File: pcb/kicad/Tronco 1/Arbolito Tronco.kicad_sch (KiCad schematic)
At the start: 18 parts, among them U1 WS2812B, U10 WS2812B, U11 WS2812B, U12 WS2812B, U2 WS2812B, U3 WS2812B, U4 WS2812B, U5 WS2812B, U6 WS2812B, U7 WS2812B, U8 WS2812B, U9 WS2812B

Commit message: Do some cleaning and add .gitignore
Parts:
- removed U10, U3, U4, U9: WS2812B, LED_SMD:LED_WS2812B_PLCC4_5.0x5.0mm_P3.2mm, symbol WB2182:WS2812B
- added J1, J2, J3, J4, J5, J6: Conn_01x01, Library:Input, symbol Connector_Generic:Conn_01x01
- added J10, J11, J12, J7, J8, J9: Conn_01x01, Library:Output, symbol Connector_Generic:Conn_01x01
- U1, U2: footprint LED_SMD:LED_WS2812B_PLCC4_5.0x5.0mm_P3.2mm -> Library:LED_WS2812B_PLCC4_5.0x5.0mm_P3.2mm
- U3: renamed from U5; footprint LED_SMD:LED_WS2812B_PLCC4_5.0x5.0mm_P3.2mm -> Library:LED_WS2812B_PLCC4_5.0x5.0mm_P3.2mm
- U4: renamed from U6; footprint LED_SMD:LED_WS2812B_PLCC4_5.0x5.0mm_P3.2mm -> Library:LED_WS2812B_PLCC4_5.0x5.0mm_P3.2mm
- U5: renamed from U7; footprint LED_SMD:LED_WS2812B_PLCC4_5.0x5.0mm_P3.2mm -> Library:LED_WS2812B_PLCC4_5.0x5.0mm_P3.2mm
- U6: renamed from U8; footprint LED_SMD:LED_WS2812B_PLCC4_5.0x5.0mm_P3.2mm -> Library:LED_WS2812B_PLCC4_5.0x5.0mm_P3.2mm
- U7: renamed from U11; footprint LED_SMD:LED_WS2812B_PLCC4_5.0x5.0mm_P3.2mm -> Library:LED_WS2812B_PLCC4_5.0x5.0mm_P3.2mm
- U8: renamed from U12; footprint LED_SMD:LED_WS2812B_PLCC4_5.0x5.0mm_P3.2mm -> Library:LED_WS2812B_PLCC4_5.0x5.0mm_P3.2mm
- renumbered C11 to C1, C12 to C2, C13 to C3, C14 to C4, C15 to C5, C16 to C6
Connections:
- net +5V: now also J10.1 (Pin_1), J3.1 (Pin_1), J4.1 (Pin_1), J9.1 (Pin_1)
- net DIN: now also J1.1 (Pin_1), J2.1 (Pin_1)
- net Dout: now also J7.1 (Pin_1), J8.1 (Pin_1)
- net GND: now also J11.1 (Pin_1), J12.1 (Pin_1), J5.1 (Pin_1), J6.1 (Pin_1)
- net at U2.2 (DOUT): now also U3.4 (DIN)
- net at U6.2 (DOUT): now also U7.4 (DIN)

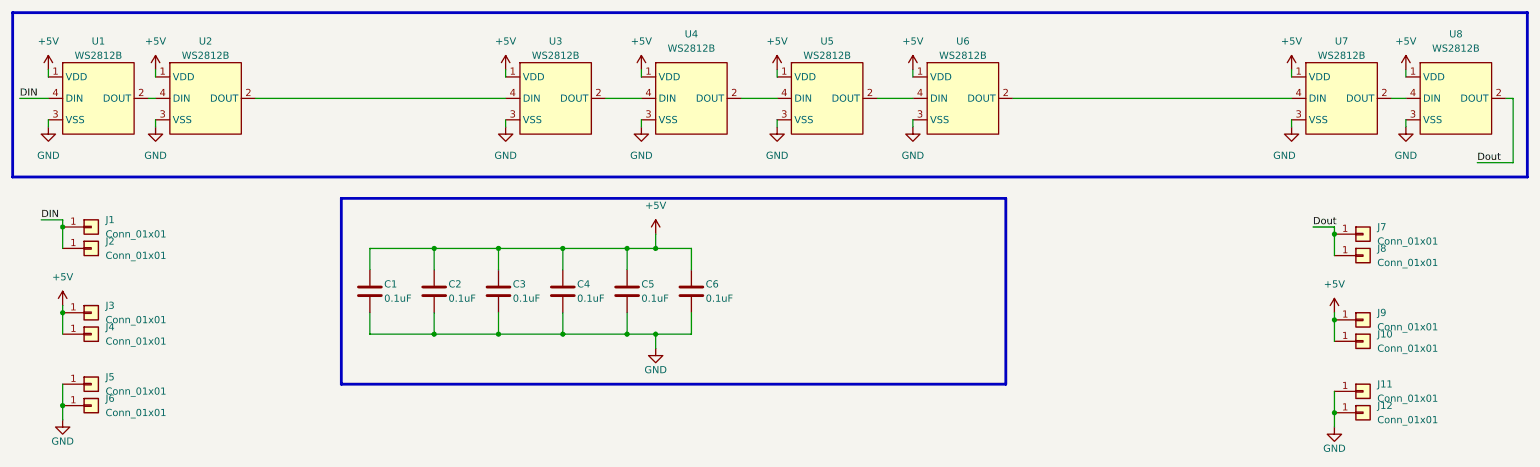
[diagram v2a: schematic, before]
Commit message: DRC Errors fixeds
The WS218B double footprint was remade in order to avoid DRC errors :3
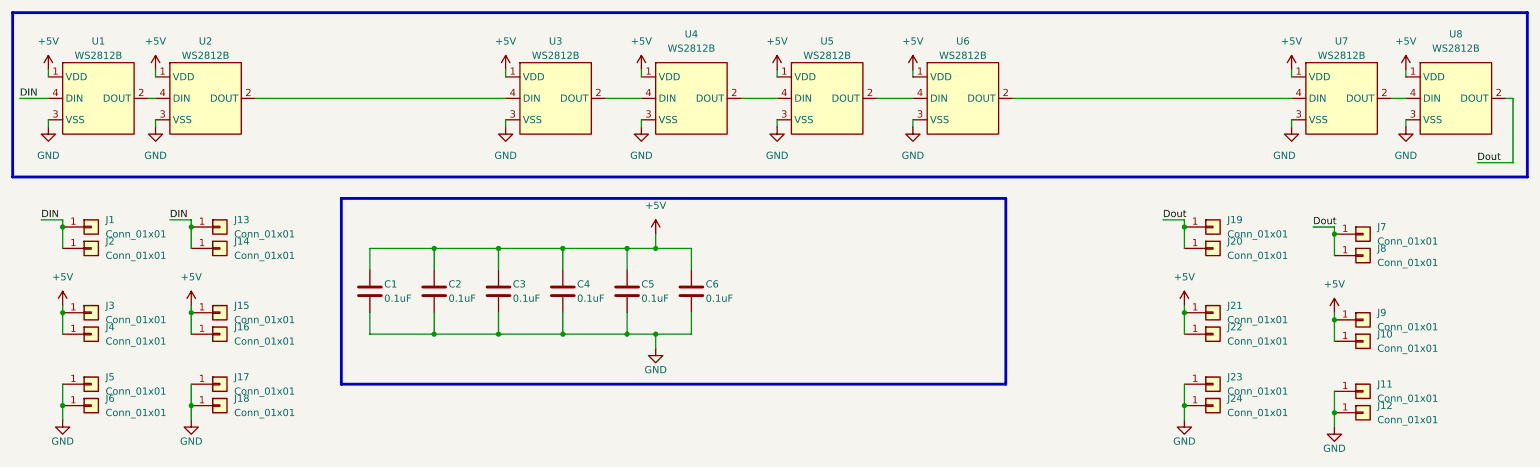
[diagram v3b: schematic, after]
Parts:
- added J13, J14, J15, J16, J17, J18: Conn_01x01, Library:Input, symbol Connector_Generic:Conn_01x01
- added J19, J20, J21, J22, J23, J24: Conn_01x01, Library:Output, symbol Connector_Generic:Conn_01x01
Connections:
- net +5V: now also J15.1 (Pin_1), J16.1 (Pin_1), J21.1 (Pin_1), J22.1 (Pin_1)
- net DIN: now also J13.1 (Pin_1), J14.1 (Pin_1)
- net Dout: now also J19.1 (Pin_1), J20.1 (Pin_1)
- net GND: now also J17.1 (Pin_1), J18.1 (Pin_1), J23.1 (Pin_1), J24.1 (Pin_1)
